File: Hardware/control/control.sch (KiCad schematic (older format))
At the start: 65 parts, among them J1 Conn_02x12_Odd_Even

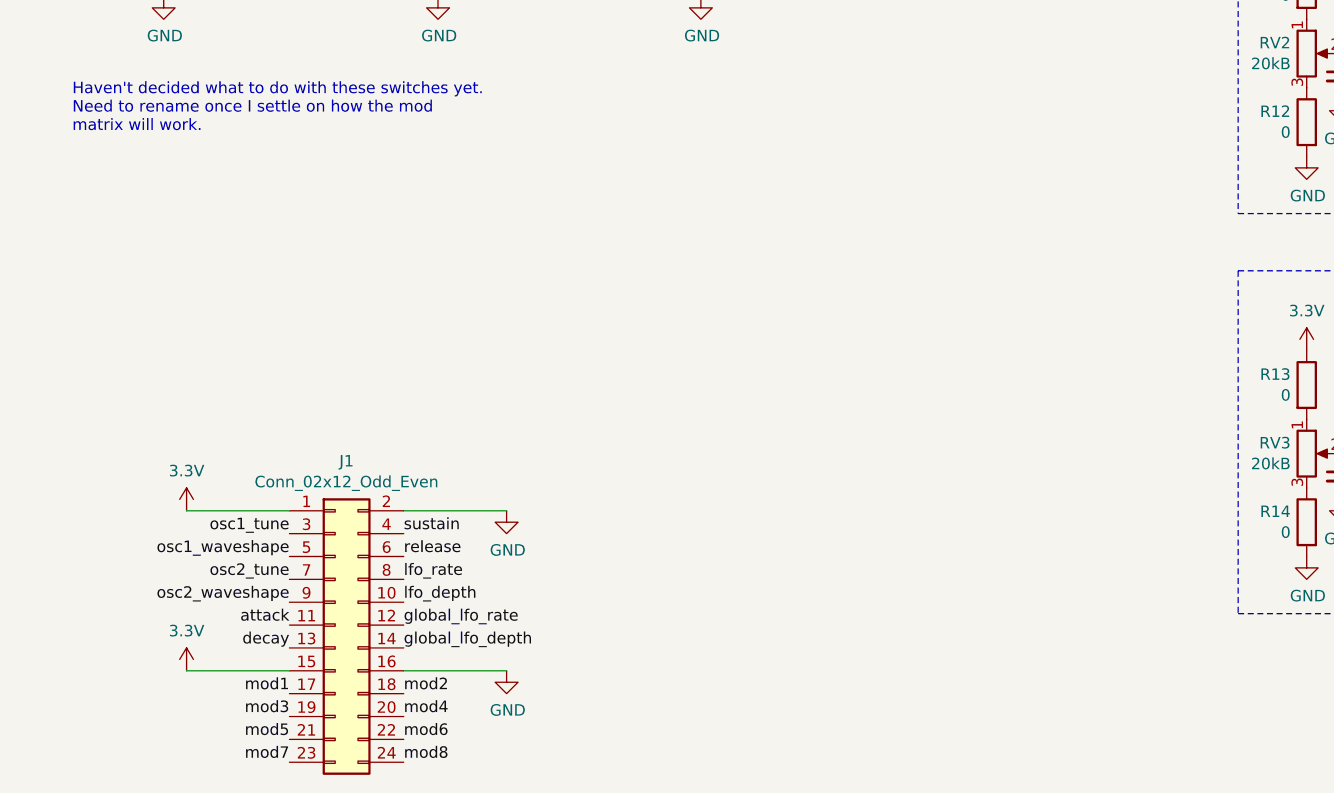
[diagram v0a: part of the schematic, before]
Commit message: initial routing complete. Still need to do ground plane pours. There are still some issues with incorrect footprints.
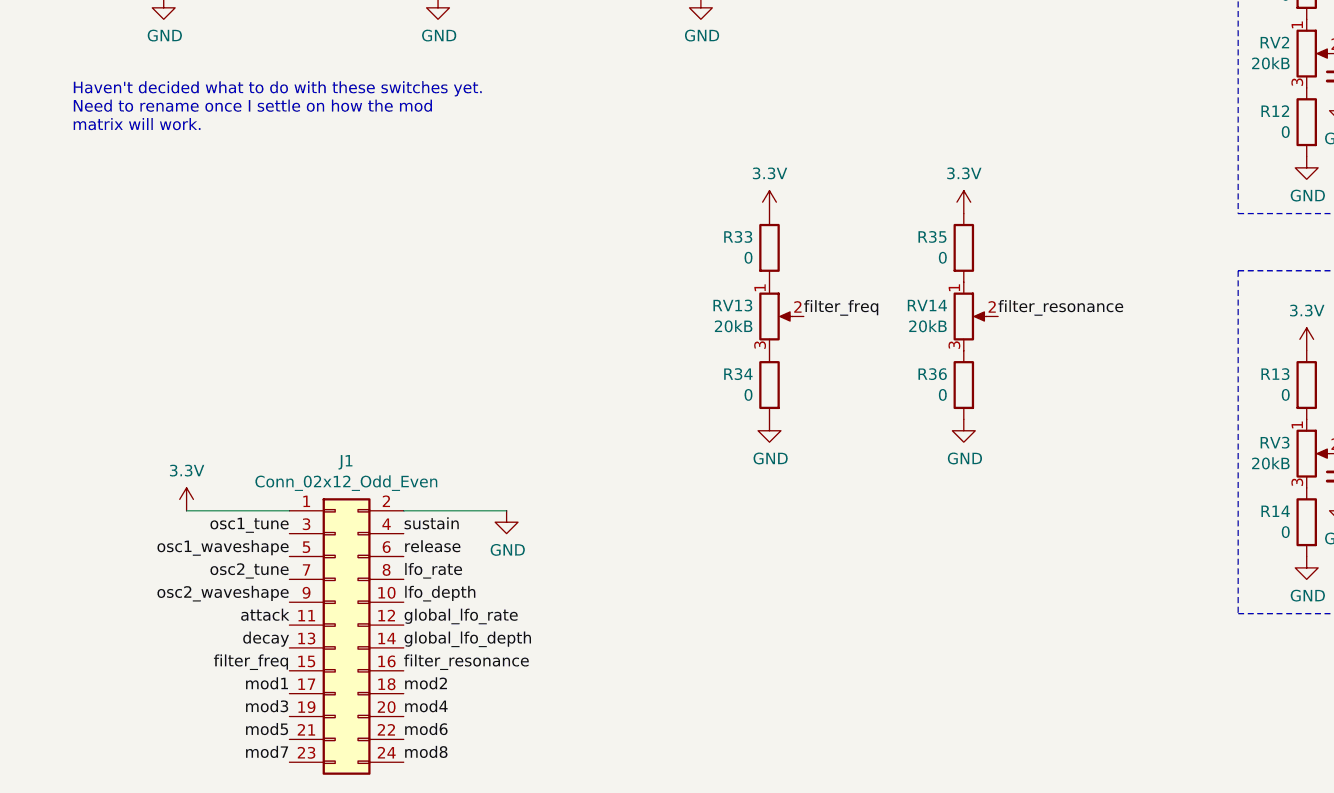
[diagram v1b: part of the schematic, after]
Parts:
- added R33, R34, R35, R36: 0, SparkFun-Passives:0805, symbol Device:R
- added RV13, RV14: 20kB, Potentiometer_THT:Potentiometer_Alps_RK09K_Single_Vertical, symbol Device:R_POT
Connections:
- net 3.3V: now also R33.1, R35.1; no longer J1.15 (Pin_15)
- net GND: now also R34.2, R36.2; no longer J1.16 (Pin_16)
- new net: R33.2, RV13.1
- new net: R34.1, RV13.3
- new net: R35.2, RV14.1
- new net: R36.1, RV14.3
- new net filter_freq: J1.15 (Pin_15), RV13.2
- new net filter_resonance: J1.16 (Pin_16), RV14.2
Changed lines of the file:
@@
 global_lfo_depth
-$Comp
-L Connector_Generic:Conn_02x12_Odd_Even J1
-U 1 1 5DDCCD44
-P 3450 6350
-F 0 "J1" H 3500 7067 50  0000 C CNN
-F 1 "Conn_02x12_Odd_Even" H 3500 6976 50  0000 C CNN
-F 2 "SparkFun-Connectors:2X12" H 3450 6350 50  0001 C CNN
-F 3 "~" H 3450 6350 50  0001 C CNN
-	1    3450 6350
-	1    0    0    -1
-$EndComp
 $Comp
 L SparkFun-Aesthetics:3.3V #SUPPLY?
@@
 Wire Wire Line
 	4200 5850 3750 5850
-$Comp
-L power:GND #PWR?
-U 1 1 5DDCD851
-P 4200 6550
-AR Path="/5DDBDEEA/5DDCD851" Ref="#PWR?"  Part="1"
-AR Path="/5DDCB333/5DDCD851" Ref="#PWR?"  Part="1"
-AR Path="/5DDCD851" Ref="#PWR0126"  Part="1"
-F 0 "#PWR0126" H 4200 6300 50  0001 C CNN
-F 1 "GND" H 4205 6377 50  0000 C CNN
-F 2 "" H 4200 6550 50  0001 C CNN
-F 3 "" H 4200 6550 50  0001 C CNN
-	1    4200 6550
-	1    0    0    -1
-$EndComp
-Wire Wire Line
-	4200 6550 3750 6550
-$Comp
-L SparkFun-Aesthetics:3.3V #SUPPLY?
-U 1 1 5DDCD9C6
-P 2800 6550
-AR Path="/5DDBDEEA/5DDCD9C6" Ref="#SUPPLY?"  Part="1"
-AR Path="/5DDCB333/5DDCD9C6" Ref="#SUPPLY?"  Part="1"
-AR Path="/5DDCD9C6" Ref="#SUPPLY0114"  Part="1"
-F 0 "#SUPPLY0114" H 2800 6550 50  0001 L BNN
-F 1 "3.3V" H 2800 6724 50  0000 C CNN
-F 2 "" H 2800 6550 50  0001 C CNN
-F 3 "" H 2800 6550 50  0001 C CNN
-	1    2800 6550
-	1    0    0    -1
-$EndComp
-Wire Wire Line
-	2800 6550 3250 6550
 Wire Wire Line
 	2800 5850 3250 5850
@@
 Text Notes 2300 4200 0    50   ~ 0
 Haven't decided what to do with these switches yet.\nNeed to rename once I settle on how the mod\nmatrix will work.
+$Comp
+L SparkFun-Aesthetics:3.3V #SUPPLY?
+U 1 1 5DDDDEAA
+P 5350 4550
+AR Path="/5DDBDEEA/5DDDDEAA" Ref="#SUPPLY?"  Part="1"
+AR Path="/5DDCB333/5DDDDEAA" Ref="#SUPPLY?"  Part="1"
+AR Path="/5DDDDEAA" Ref="#SUPPLY0114"  Part="1"
+F 0 "#SUPPLY0114" H 5350 4550 50  0001 L BNN
+F 1 "3.3V" H 5350 4724 50  0000 C CNN
+F 2 "" H 5350 4550 50  0001 C CNN
+F 3 "" H 5350 4550 50  0001 C CNN
+	1    5350 4550
+	1    0    0    -1
+$EndComp
+$Comp
+L Device:R R?
+U 1 1 5DDDDEB0
+P 5350 4700
+AR Path="/5DDBDEEA/5DDDDEB0" Ref="R?"  Part="1"
+AR Path="/5DDCB333/5DDDDEB0" Ref="R?"  Part="1"
+AR Path="/5DDDDEB0" Ref="R33"  Part="1"
+F 0 "R33" H 5280 4746 50  0000 R CNN
+F 1 "0" H 5280 4655 50  0000 R CNN
+F 2 "SparkFun-Passives:0805" V 5280 4700 50  0001 C CNN
+F 3 "~" H 5350 4700 50  0001 C CNN
+	1    5350 4700
+	1    0    0    -1
+$EndComp
+$Comp
+L Device:R_POT RV?
+U 1 1 5DDDDEB6
+P 5350 5000
+AR Path="/5DDBDEEA/5DDDDEB6" Ref="RV?"  Part="1"
+AR Path="/5DDCB333/5DDDDEB6" Ref="RV?"  Part="1"
+AR Path="/5DDDDEB6" Ref="RV13"  Part="1"
+F 0 "RV13" H 5280 5046 50  0000 R CNN
+F 1 "20kB" H 5280 4955 50  0000 R CNN
+F 2 "Potentiometer_THT:Potentiometer_Alps_RK09K_Single_Vertical" H 5350 5000 50  0001 C CNN
+F 3 "~" H 5350 5000 50  0001 C CNN
+	1    5350 5000
+	1    0    0    -1
+$EndComp
+$Comp
+L Device:R R?
+U 1 1 5DDDDEBC
+P 5350 5300
+AR Path="/5DDBDEEA/5DDDDEBC" Ref="R?"  Part="1"
+AR Path="/5DDCB333/5DDDDEBC" Ref="R?"  Part="1"
+AR Path="/5DDDDEBC" Ref="R34"  Part="1"
+F 0 "R34" H 5420 5346 50  0000 L CNN
+F 1 "0" H 5420 5255 50  0000 L CNN
+F 2 "SparkFun-Passives:0805" V 5280 5300 50  0001 C CNN
+F 3 "~" H 5350 5300 50  0001 C CNN
+	1    5350 5300
+	-1   0    0    -1
+$EndComp
+$Comp
+L power:GND #PWR?
+U 1 1 5DDDDEC2
+P 5350 5450
+AR Path="/5DDBDEEA/5DDDDEC2" Ref="#PWR?"  Part="1"
+AR Path="/5DDCB333/5DDDDEC2" Ref="#PWR?"  Part="1"
+AR Path="/5DDDDEC2" Ref="#PWR0126"  Part="1"
+F 0 "#PWR0126" H 5350 5200 50  0001 C CNN
+F 1 "GND" H 5355 5277 50  0000 C CNN
+F 2 "" H 5350 5450 50  0001 C CNN
+F 3 "" H 5350 5450 50  0001 C CNN
+	1    5350 5450
+	1    0    0    -1
+$EndComp
+$Comp
+L SparkFun-Aesthetics:3.3V #SUPPLY?
+U 1 1 5DDDE35B
+P 6200 4550
+AR Path="/5DDBDEEA/5DDDE35B" Ref="#SUPPLY?"  Part="1"
+AR Path="/5DDCB333/5DDDE35B" Ref="#SUPPLY?"  Part="1"
+AR Path="/5DDDE35B" Ref="#SUPPLY0123"  Part="1"
+F 0 "#SUPPLY0123" H 6200 4550 50  0001 L BNN
+F 1 "3.3V" H 6200 4724 50  0000 C CNN
+F 2 "" H 6200 4550 50  0001 C CNN
+F 3 "" H 6200 4550 50  0001 C CNN
+	1    6200 4550
+	1    0    0    -1
+$EndComp
+$Comp
+L Device:R R?
+U 1 1 5DDDE361
+P 6200 4700
+AR Path="/5DDBDEEA/5DDDE361" Ref="R?"  Part="1"
+AR Path="/5DDCB333/5DDDE361" Ref="R?"  Part="1"
+AR Path="/5DDDE361" Ref="R35"  Part="1"
+F 0 "R35" H 6130 4746 50  0000 R CNN
+F 1 "0" H 6130 4655 50  0000 R CNN
+F 2 "SparkFun-Passives:0805" V 6130 4700 50  0001 C CNN
+F 3 "~" H 6200 4700 50  0001 C CNN
+	1    6200 4700
+	1    0    0    -1
+$EndComp
+$Comp
+L Device:R_POT RV?
+U 1 1 5DDDE367
+P 6200 5000
+AR Path="/5DDBDEEA/5DDDE367" Ref="RV?"  Part="1"
+AR Path="/5DDCB333/5DDDE367" Ref="RV?"  Part="1"
+AR Path="/5DDDE367" Ref="RV14"  Part="1"
+F 0 "RV14" H 6130 5046 50  0000 R CNN
+F 1 "20kB" H 6130 4955 50  0000 R CNN
+F 2 "Potentiometer_THT:Potentiometer_Alps_RK09K_Single_Vertical" H 6200 5000 50  0001 C CNN
+F 3 "~" H 6200 5000 50  0001 C CNN
+	1    6200 5000
+	1    0    0    -1
+$EndComp
+$Comp
+L Device:R R?
+U 1 1 5DDDE36D
+P 6200 5300
+AR Path="/5DDBDEEA/5DDDE36D" Ref="R?"  Part="1"
+AR Path="/5DDCB333/5DDDE36D" Ref="R?"  Part="1"
+AR Path="/5DDDE36D" Ref="R36"  Part="1"
+F 0 "R36" H 6270 5346 50  0000 L CNN
+F 1 "0" H 6270 5255 50  0000 L CNN
+F 2 "SparkFun-Passives:0805" V 6130 5300 50  0001 C CNN
+F 3 "~" H 6200 5300 50  0001 C CNN
+	1    6200 5300
+	-1   0    0    -1
+$EndComp
+$Comp
+L power:GND #PWR?
+U 1 1 5DDDE373
+P 6200 5450
+AR Path="/5DDBDEEA/5DDDE373" Ref="#PWR?"  Part="1"
+AR Path="/5DDCB333/5DDDE373" Ref="#PWR?"  Part="1"
+AR Path="/5DDDE373" Ref="#PWR0135"  Part="1"
+F 0 "#PWR0135" H 6200 5200 50  0001 C CNN
+F 1 "GND" H 6205 5277 50  0000 C CNN
+F 2 "" H 6200 5450 50  0001 C CNN
+F 3 "" H 6200 5450 50  0001 C CNN
+	1    6200 5450
+	1    0    0    -1
+$EndComp
+Text Label 5500 5000 0    50   ~ 0
+filter_freq
+Text Label 6350 5000 0    50   ~ 0
+filter_resonance
+$Comp
+L Connector_Generic:Conn_02x12_Odd_Even J1
+U 1 1 5DDCCD44
+P 3450 6350
+F 0 "J1" H 3500 7067 50  0000 C CNN
+F 1 "Conn_02x12_Odd_Even" H 3500 6976 50  0000 C CNN
+F 2 "SparkFun-Connectors:2X12" H 3450 6350 50  0001 C CNN
+F 3 "~" H 3450 6350 50  0001 C CNN
+	1    3450 6350
+	1    0    0    -1
+$EndComp
+Text Label 3250 6550 2    50   ~ 0
+filter_freq
+Text Label 3750 6550 0    50   ~ 0
+filter_resonance
 $EndSCHEMATC
